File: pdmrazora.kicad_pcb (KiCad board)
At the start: 2 copper layers, 109 x 98 mm, 54 parts, among them J1 6473418-1, J2 M6_VBAT, J3 M6_GND, M1000 Module:mega-mcu144/0.7, U1 BTS50010-1TAD, U11 BTS7004-1EPP, U12 BTS7004-1EPP, U13 BTS7004-1EPP, U14 BTS7004-1EPP, U15 BTS7004-1EPP, U16 BTS7004-1EPP, U17 BTS7004-1EPP, U18 BTS7004-1EPP, U2 BTS50010-1TAD, U3 BTS50010-1TAD, U4 BTS50010-1TAD

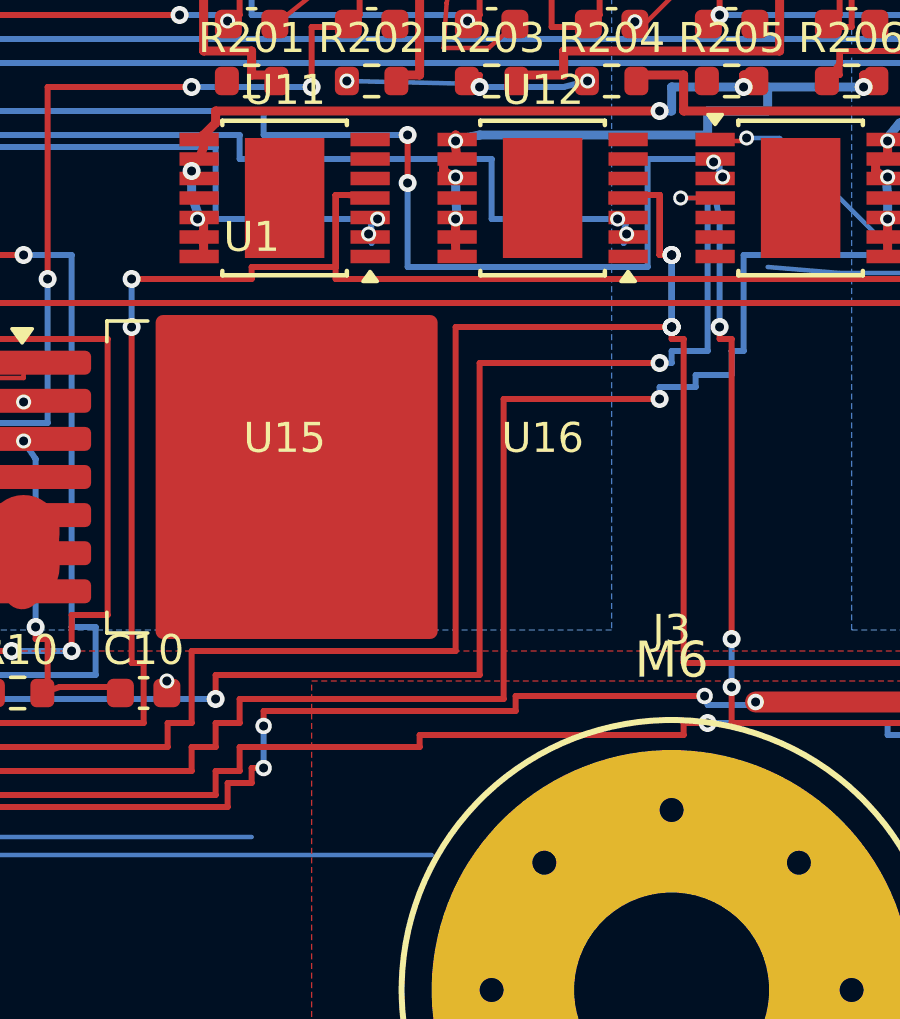
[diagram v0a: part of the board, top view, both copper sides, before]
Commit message: Land ADIO6 through the GND pour neck.
Jog OUT_IO7 off x=72.4, run ADIO6 onto the driver, and stitch the
cut-off B.Cu GND island into the J3 pour so the hop does not add a ratsnest.

Co-authored-by: Quintin <quintinbannink42@users.noreply.github.com>
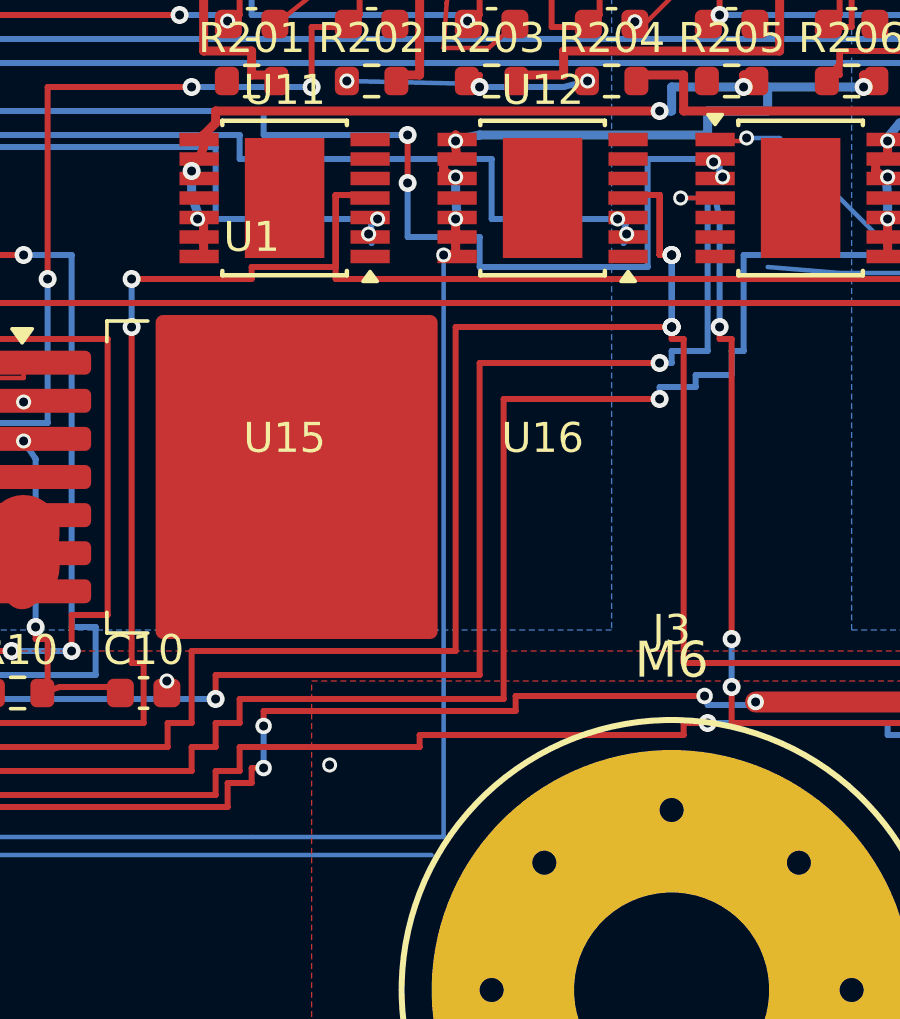
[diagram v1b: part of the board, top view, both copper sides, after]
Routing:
- net ADIO6: track 125.5 -> 151.7 mm, vias 4 -> 5
- net GND: vias 29 -> 30
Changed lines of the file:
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@@
 	)
 	(via
+		(at 68.6 79)
+		(size 0.5)
+		(drill 0.3)
+		(layers "F.Cu" "B.Cu")
+		(net 2)
+	)
+	(via
 		(at 81.4 41)
 		(size 0.5)
@@
 	)
 	(segment
+		(start 72.4 62)
+		(end 72.8 62)
+		(width 0.15)
+		(layer "F.Cu")
+		(net 17)
+	)
+	(segment
 		(start 72.8 60.8)
 		(end 72.8 61.2)
@@
 	)
 	(via
+		(at 72.4 62)
+		(size 0.5)
+		(drill 0.3)
+		(layers "F.Cu" "B.Cu")
+		(net 17)
+	)
+	(via
 		(at 72.8 58.2)
 		(size 0.5)
@@
 	)
 	(segment
+		(start 72.4 81.4)
+		(end 72.4 62)
+		(width 0.15)
+		(layer "B.Cu")
+		(net 17)
+	)
+	(segment
 		(start 20.1 60.4)
 		(end 20.1 73)
@@
 	)
 	(segment
+		(start 66 81.4)
+		(end 72.4 81.4)
+		(width 0.15)
+		(layer "B.Cu")
+		(net 17)
+	)
+	(segment
 		(start 72.85 58.15)
 		(end 72.8 58.2)
@@
 	)
 	(segment
-		(start 81.6 54)
-		(end 92.8 54)
+		(start 92.8 54)
+		(end 92.8 62.8)
 		(width 0.2)
 		(layer "B.Cu")
@@
 	)
 	(segment
-		(start 92.8 54)
-		(end 92.8 62.8)
+		(start 81.6 54)
+		(end 92.8 54)
 		(width 0.2)
 		(layer "B.Cu")
@@
 	)
 	(segment
+		(start 79.2 62.4)
+		(end 73.6 62.4)
+		(width 0.2)
+		(layer "B.Cu")
+		(net 54)
+	)
+	(segment
 		(start 46.8 52.8)
 		(end 46.4 52.8)
@@
 	)
 	(segment
-		(start 81.6 59.2)
-		(end 81.45 59.45)
+		(start 71.2 61.4)
+		(end 71.2 59.6)
 		(width 0.2)
 		(layer "B.Cu")
@@
 	)
 	(segment
-		(start 66.4 58)
-		(end 66.4 57.2)
+		(start 81.6 59.2)
+		(end 81.45 59.45)
 		(width 0.2)
 		(layer "B.Cu")
@@
 	)
 	(segment
-		(start 79.2 62.4)
-		(end 71.2 62.4)
+		(start 66.4 58)
+		(end 66.4 57.2)
 		(width 0.2)
 		(layer "B.Cu")
@@
 	)
 	(segment
+		(start 73.6 61.4)
+		(end 71.2 61.4)
+		(width 0.2)
+		(layer "B.Cu")
+		(net 54)
+	)
+	(segment
 		(start 66.4 57.2)
 		(end 46.8 57.2)
@@
 	)
 	(segment
-		(start 71.2 62.4)
-		(end 71.2 59.6)
+		(start 73.6 62.4)
+		(end 73.6 61.4)
 		(width 0.2)
 		(layer "B.Cu")
@@
 			)
 		)
+	)
+	(zone
+		(net 0)
+		(net_name "")
+		(layer "B.Cu")
+		(hatch edge 0.5)
+		(connect_pads
+			(clearance 0)
+		)
+		(min_thickness 0.25)
+		(filled_areas_thickness no)
+		(keepout
+			(tracks allowed)
+			(vias allowed)
+			(pads allowed)
+			(copperpour not_allowed)
+			(footprints allowed)
+		)
+		(fill
+			(thermal_gap 0.5)
+			(thermal_bridge_width 0.5)
+		)
+		(polygon
+			(pts
+				(xy 71 63) (xy 75 63) (xy 75 81) (xy 71 81)
+			)
+		)

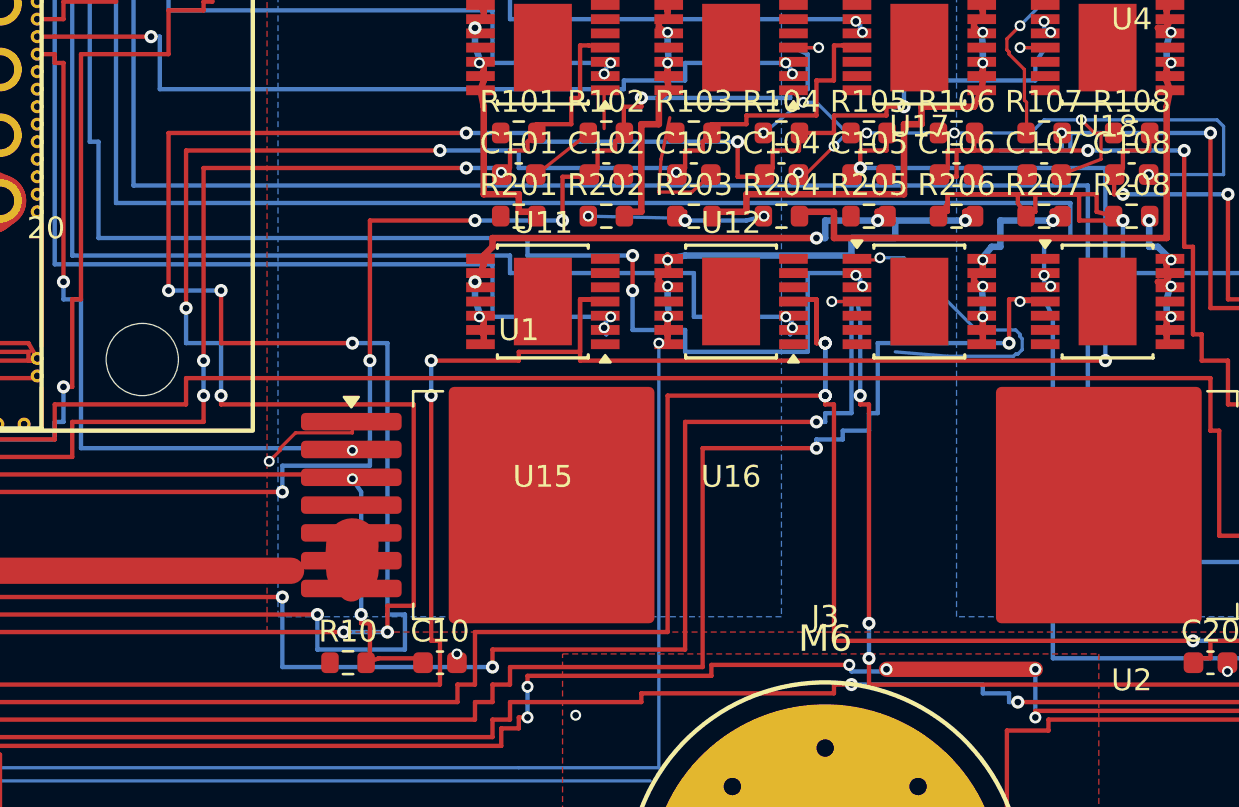
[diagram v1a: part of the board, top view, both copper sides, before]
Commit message: Land IN_RES2 and stitch R10, C105, and C106.
Widen the B.Cu slot so IN_RES2, C105, and C106 can via onto copper
already on those nets, and jog the R10 slot so that pad ties to the
C10 via. Unconnected 50 to 46. F1, the keepout, VBAT islands, and the
358 mask openings stay put.

Co-authored-by: Quintin <quintinbannink42@users.noreply.github.com>
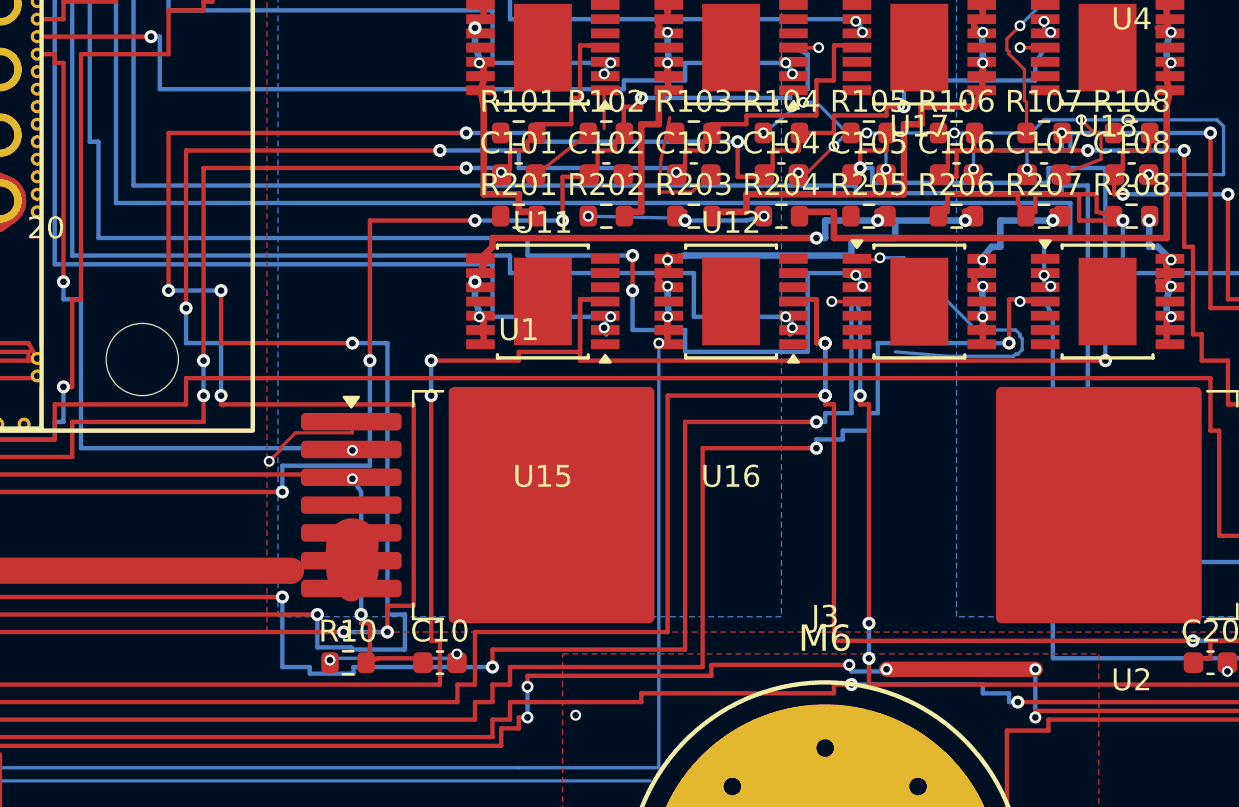
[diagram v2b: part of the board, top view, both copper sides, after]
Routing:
- net GND: track 146.8 -> 156.0 mm, vias 30 -> 33
- net IN_RES2: track 172.4 -> 173.9 mm, vias 10 -> 11
- net IN_O2S2: track 126.2 -> 127.5 mm
- net OUT_PWM2: track 89.0 -> 89.7 mm
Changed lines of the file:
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@@
 	)
 	(segment
-		(start 66.8 54.3)
-		(end 69.2 52.4)
-		(width 0.15)
-		(layer "F.Cu")
-		(net 2)
-	)
-	(segment
 		(start 74.8 54.3)
 		(end 73.9 55.1)
@@
 	)
 	(segment
+		(start 66.8 54.3)
+		(end 69.2 52.4)
+		(width 0.15)
+		(layer "F.Cu")
+		(net 2)
+	)
+	(segment
 		(start 101.6 73.2)
 		(end 102.6 73.2)
@@
 	)
 	(via
+		(at 82.775 54.05)
+		(size 0.5)
+		(drill 0.3)
+		(layers "F.Cu" "B.Cu")
+		(net 2)
+	)
+	(via
 		(at 103.9 6.2)
 		(size 0.5)
@@
 	)
 	(via
+		(at 57.375 76.48)
+		(size 0.5)
+		(drill 0.3)
+		(layers "F.Cu" "B.Cu")
+		(net 2)
+	)
+	(via
 		(at 82.5 58.1)
 		(size 0.5)
@@
 		(net 2)
 	)
+	(via
+		(at 86.775 54.05)
+		(size 0.5)
+		(drill 0.3)
+		(layers "F.Cu" "B.Cu")
+		(net 2)
+	)
 	(segment
 		(start 94.78 54.3)
@@
 	)
 	(segment
+		(start 57.375 76.4)
+		(end 63.175 76.4)
+		(width 0.15)
+		(layer "B.Cu")
+		(net 2)
+	)
+	(segment
 		(start 91.7 51.8)
 		(end 90 51.8)
@@
 	)
 	(segment
+		(start 86.775 54.05)
+		(end 86.775 52.4)
+		(width 0.15)
+		(layer "B.Cu")
+		(net 2)
+	)
+	(segment
 		(start 105.4 61.8)
 		(end 105.6 61.6)
@@
 	)
 	(segment
+		(start 57.375 76.48)
+		(end 57.375 76.4)
+		(width 0.15)
+		(layer "B.Cu")
+		(net 2)
+	)
+	(segment
+		(start 82.775 54.05)
+		(end 82.775 52.4)
+		(width 0.15)
+		(layer "B.Cu")
+		(net 2)
+	)
+	(segment
 		(start 97.9 51.8)
 		(end 91.9 51.8)
@@
 	)
 	(segment
-		(start 60.8 76)
-		(end 56.8 76)
+		(start 56.8 75.9)
+		(end 58.35 75.9)
 		(width 0.2)
 		(layer "B.Cu")
@@
 	)
 	(segment
+		(start 56.8 74.4)
+		(end 56.8 75.9)
+		(width 0.2)
+		(layer "B.Cu")
+		(net 31)
+	)
+	(segment
 		(start 58.4 62)
 		(end 60 62)
@@
 	)
 	(segment
+		(start 58.35 76)
+		(end 60.8 76)
+		(width 0.2)
+		(layer "B.Cu")
+		(net 31)
+	)
+	(segment
 		(start 66.8 52.4)
 		(end 63.6 52.4)
@@
 	)
 	(segment
-		(start 56.8 76)
-		(end 56.8 74.4)
+		(start 25.6 66.4)
+		(end 25.50001 65.7)
 		(width 0.2)
 		(layer "B.Cu")
@@
 	)
 	(segment
-		(start 25.6 66.4)
-		(end 25.50001 65.7)
+		(start 58.35 75.9)
+		(end 58.35 76)
 		(width 0.2)
 		(layer "B.Cu")
@@
 	)
 	(segment
+		(start 82.15 54.68)
+		(end 90.2 54.68)
+		(width 0.2)
+		(layer "B.Cu")
+		(net 32)
+	)
+	(segment
+		(start 82.15 54)
+		(end 82.15 54.68)
+		(width 0.2)
+		(layer "B.Cu")
+		(net 32)
+	)
+	(segment
 		(start 26.8 66.4)
 		(end 26.700008 65.7)
@@
 	)
 	(segment
+		(start 90.2 54)
+		(end 92.8 54)
+		(width 0.2)
+		(layer "B.Cu")
+		(net 32)
+	)
+	(segment
 		(start 92.8 54)
 		(end 92.8 62.8)
@@
 	(segment
 		(start 81.6 54)
-		(end 92.8 54)
+		(end 82.15 54)
 		(width 0.2)
 		(layer "B.Cu")
@@
 	)
 	(segment
+		(start 90.2 54.68)
+		(end 90.2 54)
+		(width 0.2)
+		(layer "B.Cu")
+		(net 32)
+	)
+	(segment
 		(start 26.8 76)
 		(end 26.8 66.4)
@@
 	)
 	(via
+		(at 89.22 54.05)
+		(size 0.5)
+		(drill 0.3)
+		(layers "F.Cu" "B.Cu")
+		(net 36)
+	)
+	(via
 		(at 82 74.8)
 		(size 0.6)
@@
 	)
 	(segment
+		(start 58.45 77.1)
+		(end 58.45 76.8)
+		(width 0.2)
+		(layer "B.Cu")
+		(net 36)
+	)
+	(segment
 		(start 80 65.6)
 		(end 79.6 65.6)
@@
 	)
 	(segment
+		(start 56.45 76.8)
+		(end 56.45 77.1)
+		(width 0.2)
+		(layer "B.Cu")
+		(net 36)
+	)
+	(segment
 		(start 90.8 52.4)
 		(end 90.825 52.4)
@@
 	)
 	(segment
-		(start 64.8 76.8)
-		(end 55.2 76.8)
-		(width 0.2)
-		(layer "B.Cu")
-		(net 36)
-	)
-	(segment
 		(start 27.6 66.4)
 		(end 27.900008 65.7)
@@
 	)
 	(segment
+		(start 58.45 76.8)
+		(end 64.8 76.8)
+		(width 0.2)
+		(layer "B.Cu")
+		(net 36)
+	)
+	(segment
 		(start 91.2 52.4)
 		(end 97.6 52.4)
@@
 	)
 	(segment
+		(start 56.45 77.1)
+		(end 58.45 77.1)
+		(width 0.2)
+		(layer "B.Cu")
+		(net 36)
+	)
+	(segment
+		(start 55.2 76.8)
+		(end 56.45 76.8)
+		(width 0.2)
+		(layer "B.Cu")
+		(net 36)
+	)
+	(segment
 		(start 82 76.4)
 		(end 82 74.8)
@@
 	)
 	(segment
+		(start 89.22 54.05)
+		(end 89.22 53.2)
+		(width 0.15)
+		(layer "B.Cu")
+		(net 36)
+	)
+	(segment
 		(start 81.2 65.2)
 		(end 80 65.2)
@@
 	)
 	(segment
-		(start 92 54.8)
-		(end 48.4 54.8)
+		(start 81.4 54.8)
+		(end 81.4 55.15)
+		(width 0.2)
+		(layer "B.Cu")
+		(net 58)
+	)
+	(segment
+		(start 90.8 54.8)
+		(end 92 54.8)
 		(width 0.2)
 		(layer "B.Cu")
@@
 	)
 	(segment
+		(start 90.8 55.15)
+		(end 90.8 54.8)
+		(width 0.2)
+		(layer "B.Cu")
+		(net 58)
+	)
+	(segment
 		(start 92 72)
 		(end 92 54.8)
@@
 	)
 	(segment
+		(start 81.4 55.15)
+		(end 90.8 55.15)
+		(width 0.2)
+		(layer "B.Cu")
+		(net 58)
+	)
+	(segment
 		(start 101.6 71.9)
 		(end 101.65 71.94)
@@
 		(width 0.2)
 		(layer "B.Cu")
+		(net 58)
+	)
+	(segment
+		(start 48.4 54.8)
+		(end 81.4 54.8)
+		(width 0.2)
+		(layer "B.Cu")
